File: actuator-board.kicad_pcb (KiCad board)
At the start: 4 copper layers, 22 x 40 mm, 56 parts, among them J1 SERVO DCDC 5V, J10 Servo, J2 Conn_01x06, J3 Actuator1, J4 Actuator2, J5 SWD/DEBUG, J6 BATTERY, J7 CAN, J8 CAN, J9 Servo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

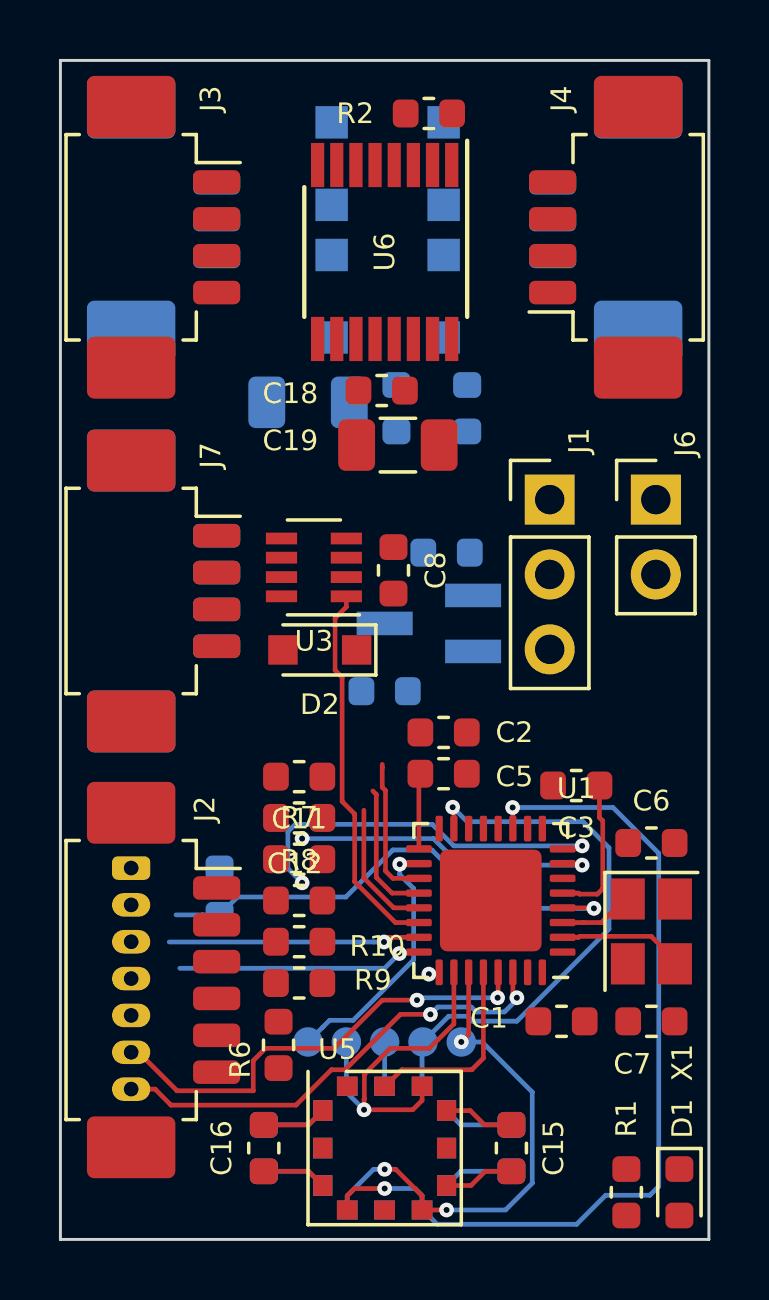
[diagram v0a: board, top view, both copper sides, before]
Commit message: layout: CAN, rearrange LED/CS1/CS2
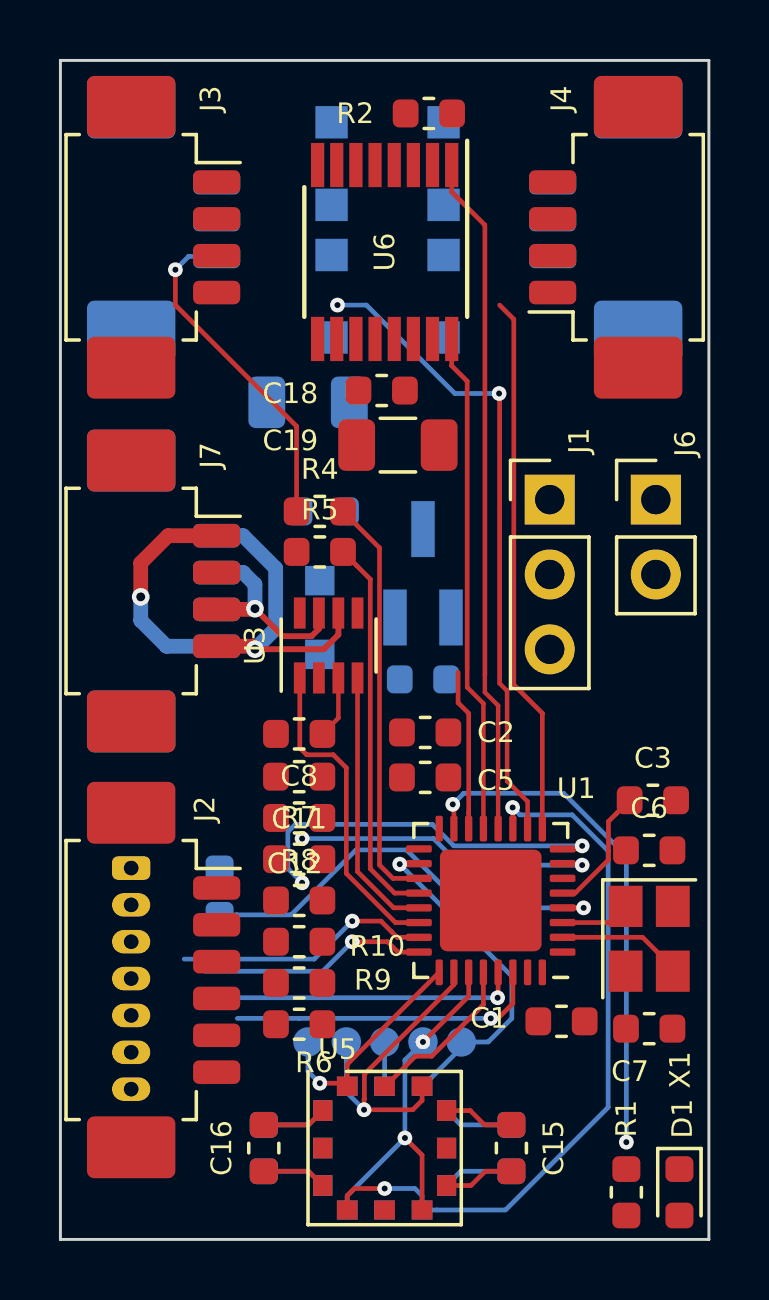
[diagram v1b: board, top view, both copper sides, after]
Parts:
- D2: moved to B.Cu
- R4, R5: moved to F.Cu
- moved R5 6.98 mm to (56.8, 76.7), turned to 0 degrees
- moved C8 6.41 mm to (56.1, 82.8), turned to 180 degrees
- moved C9 4.43 mm to (56.9, 75.3), turned to 180 degrees
- moved R4 4.36 mm to (56.8, 75.3), turned to 0 degrees
- moved U3 2.70 mm to (57.1, 79.8), turned to 90 degrees
- moved C3 2.65 mm to (68.1, 85.1), turned to 0 degrees
- moved U2 1.71 mm to (60.3, 77.4), turned to 90 degrees
- moved C10 1.36 mm to (60.3, 81.0)
- moved TP2 1.30 mm to (60.3, 93.3)
- moved TP4 1.30 mm to (61.6, 93.3)
- moved D2 1.10 mm to (56.8, 78.9), turned to 270 degrees
- moved R6 0.99 mm to (56.1, 92.7), turned to 0 degrees
- moved C5 0.64 mm to (60.4, 84.3)
- moved C2 0.62 mm to (60.4, 82.8)
- moved C6 0.26 mm to (68.0, 86.8)
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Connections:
- U1 pad 15: /SPI_CS1 -> /LED
- U1 pad 18: /SPI_CS2 -> /SPI_CS1
- U1 pad 25: /LED -> /SPI_CS2
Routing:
- net /PUMP_SOLENOID_ENABLE: track 0.00 -> 23.2 mm
- net /SOLENOID_IN2: track 0.00 -> 21.9 mm, vias 0 -> 2
- net /SOLENOID_IN1: track 0.00 -> 18.4 mm
- net /LED: track 0.38 -> 17.5 mm, vias 1 -> 2
- net /PUMP1: track 0.00 -> 17.1 mm
- net /SERVO1: track 0.00 -> 11.5 mm, vias 0 -> 1
- net Net-(J7-Pad4): track 0.00 -> 10.6 mm, vias 0 -> 1
- net Net-(R4-Pad2): track 4.90 -> 14.0 mm
- net Net-(R5-Pad2): track 4.65 -> 13.1 mm
- net +5V: track 0.00 -> 7.85 mm, vias 0 -> 1
- net /SPI_CS1: track 18.9 -> 11.7 mm
- net Net-(J7-Pad3): track 0.00 -> 6.79 mm, vias 0 -> 1
- net /PUMP2: track 0.00 -> 5.45 mm
- net /VACUUM_SENS_RESET: track 30.1 -> 24.7 mm
- net /UART1RX: track 15.9 -> 10.6 mm, vias 2 -> 1
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
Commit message: layout: power electronics, more components on F.Cu layer
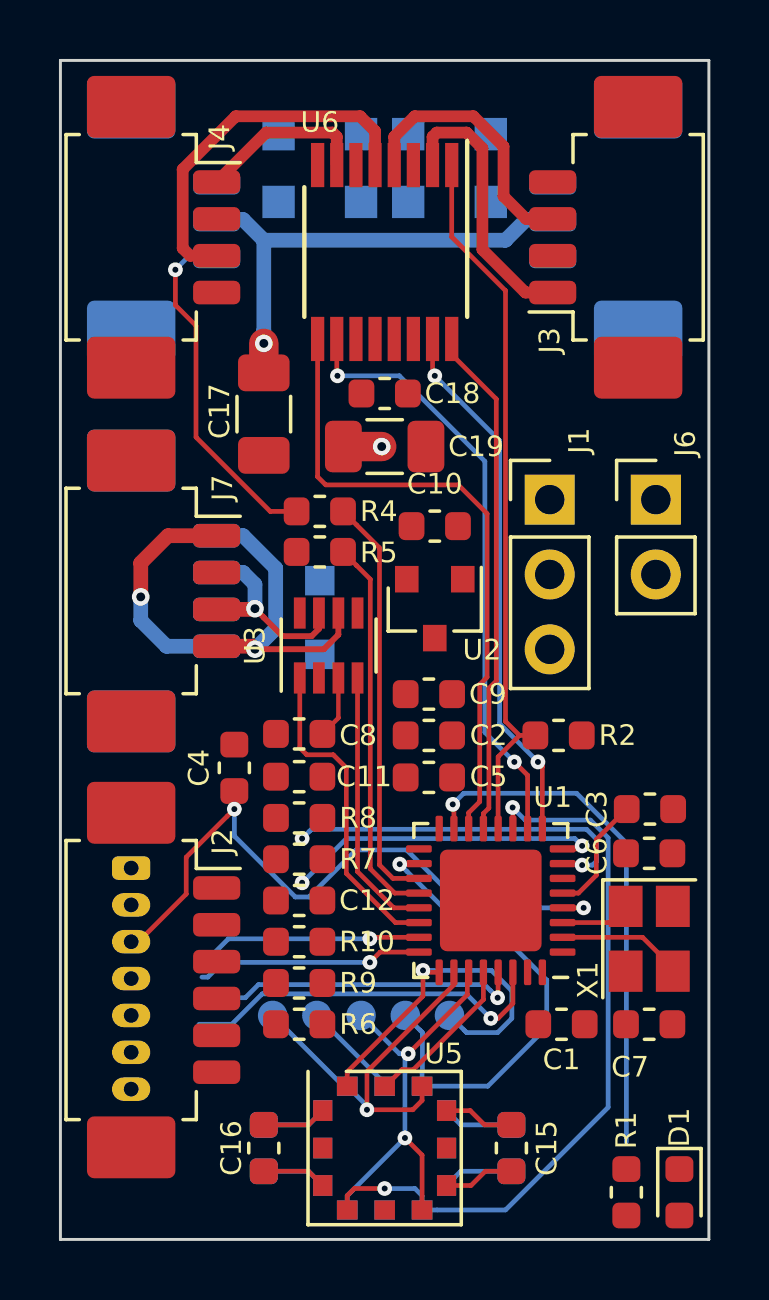
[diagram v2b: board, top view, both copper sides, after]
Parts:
- C10, C17, C4, C9: moved to F.Cu
- U2: footprint Package_TO_SOT_SMD:SOT-23_Handsoldering -> Package_TO_SOT_SMD:SOT-23; moved to F.Cu
- moved R2 21.6 mm to (64.9, 82.9), turned to 0 degrees
- moved J3 16.2 mm to (67.1, 66.0), turned to 90 degrees
- moved J4 16.2 mm to (50.9, 66.0), turned to 270 degrees
- moved C9 7.17 mm to (60.5, 81.5), turned to 0 degrees
- moved D5 6.92 mm to (56.8, 62.5), turned to 0 degrees
- moved C10 5.22 mm to (60.7, 75.8)
- moved D3 5.12 mm to (61.2, 64.8), turned to 180 degrees
- moved TP5 4.88 mm to (61.2, 92.4)
- moved D6 4.40 mm to (56.8, 64.8), turned to 0 degrees
- moved C4 4.23 mm to (53.9, 84.0)
- moved D4 4.12 mm to (61.2, 62.5), turned to 180 degrees
- moved TP3 2.66 mm to (55.2, 92.4)
- moved TP1 2.47 mm to (56.7, 92.4)
- moved TP2 2.28 mm to (58.2, 92.4)
- moved TP4 2.10 mm to (59.7, 92.4)
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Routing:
- net Net-(C17-Pad1): track 0.00 -> 34.3 mm, vias 0 -> 1
- net /PUMP2: track 5.45 -> 21.9 mm
- net Net-(D6-Pad1): track 0.00 -> 12.6 mm
- net +BATT: track 0.00 -> 11.3 mm, vias 0 -> 1
- net Net-(D3-Pad1): track 0.00 -> 9.35 mm
- net Net-(D4-Pad1): track 0.00 -> 9.05 mm
- net /RESET: track 14.8 -> 22.5 mm, vias 1 -> 2
- net Net-(D5-Pad1): track 0.00 -> 5.79 mm
- net /SPI_CS1: track 11.7 -> 16.7 mm
- net /SPI_CS2: track 7.69 -> 12.4 mm
- net /SPI_MISO: track 12.5 -> 14.6 mm
- net /ANALOG2: track 13.0 -> 10.9 mm
- net /UART1RX: track 10.6 -> 12.7 mm
- net /SPI_SCK: track 11.1 -> 13.0 mm
- net /SPI_MOSI: track 7.09 -> 8.85 mm
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
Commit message: HTSSOP motor driver, component arrangment, added MCU capacitor
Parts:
- added C20: 1uF, Capacitor_SMD:C_0603_1608Metric, F.Cu at (68.0, 84.6)
- C3: value 0.1uF -> 10nF
- D2: moved to F.Cu
- U6: footprint Package_SO:TSSOP-16_4.4x5mm_P0.65mm -> Package_SO:TSSOP-16-1EP_4.4x5mm_P0.65mm
- moved R2 11.7 mm to (63.8, 71.3)
- moved C17 11.2 mm to (66.0, 73.6), turned to 0 degrees
- moved R4 7.22 mm to (60.5, 81.5), turned to 180 degrees
- moved D2 7.18 mm to (54.8, 72.0), turned to 90 degrees
- moved C9 7.03 mm to (56.0, 76.1), turned to 270 degrees
- moved J1 6.90 mm to (64.6, 81.8), turned to 180 degrees
- moved J6 6.90 mm to (68.2, 81.8), turned to 180 degrees
- moved R5 5.04 mm to (60.5, 80.1), turned to 180 degrees
- moved U2 2.92 mm to (59.2, 76.1), turned to 180 degrees
- moved C10 1.22 mm to (61.9, 76.0), turned to 270 degrees
- moved C1 0.78 mm to (64.5, 93.3)
- moved C3 0.60 mm to (68.0, 86.0)
- moved X1 0.53 mm to (67.8, 90.3)
- moved C6 0.50 mm to (68.0, 87.4)
- moved C7 0.50 mm to (68.0, 93.2)
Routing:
- net Net-(C17-Pad1): track 34.3 -> 0.00 mm, vias 1 -> 0
- net /PUMP2: track 21.9 -> 5.04 mm
- net /SERVO1: track 12.0 -> 0.00 mm, vias 1 -> 0
- net +BATT: track 11.3 -> 0.00 mm, vias 1 -> 0
- net Net-(R4-Pad2): track 14.0 -> 7.52 mm
- net VCC: track 10.8 -> 6.72 mm
- net /RESET: track 22.5 -> 18.7 mm
- net Net-(R5-Pad2): track 13.1 -> 9.64 mm
- net /UART1RX: track 12.7 -> 15.9 mm
- net /PUMP_SOLENOID_ENABLE: track 24.3 -> 23.2 mm

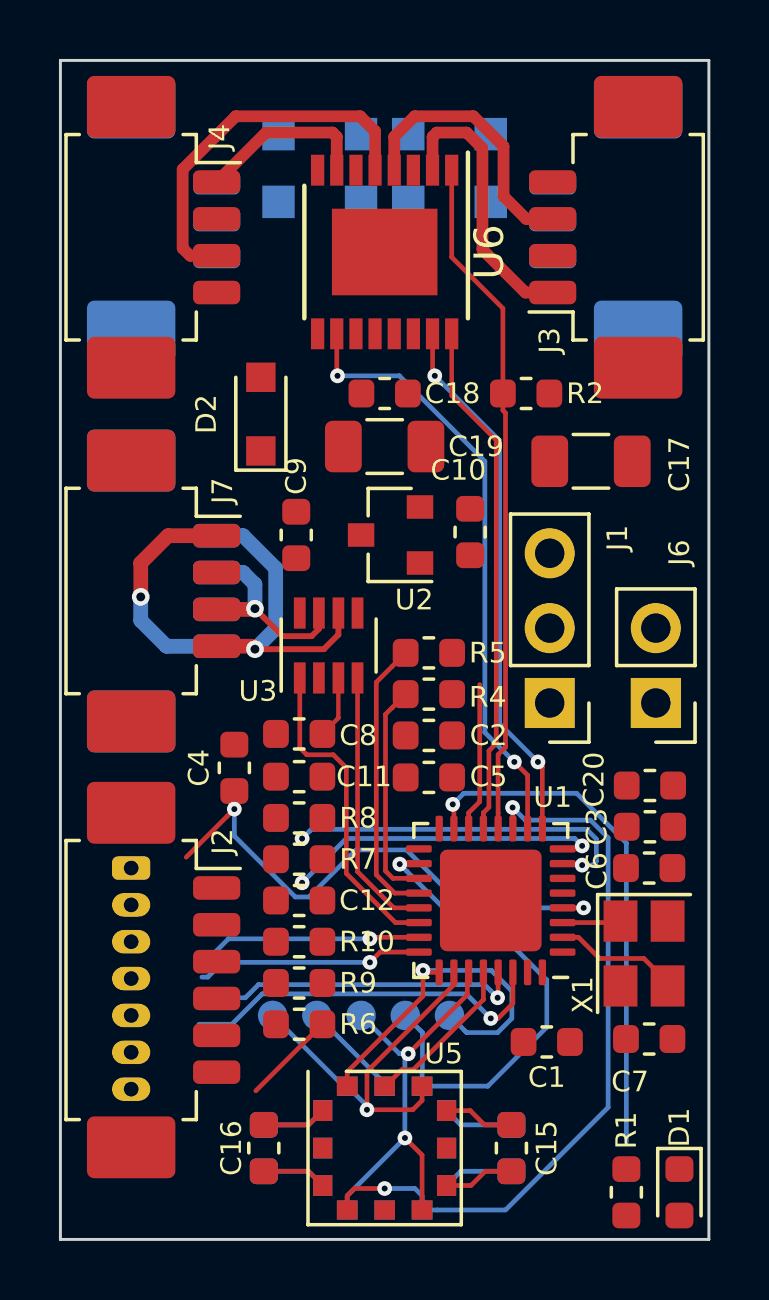
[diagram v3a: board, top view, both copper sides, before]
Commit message: Silk screen doc, ground vias, exchange servo 1 <-> 2
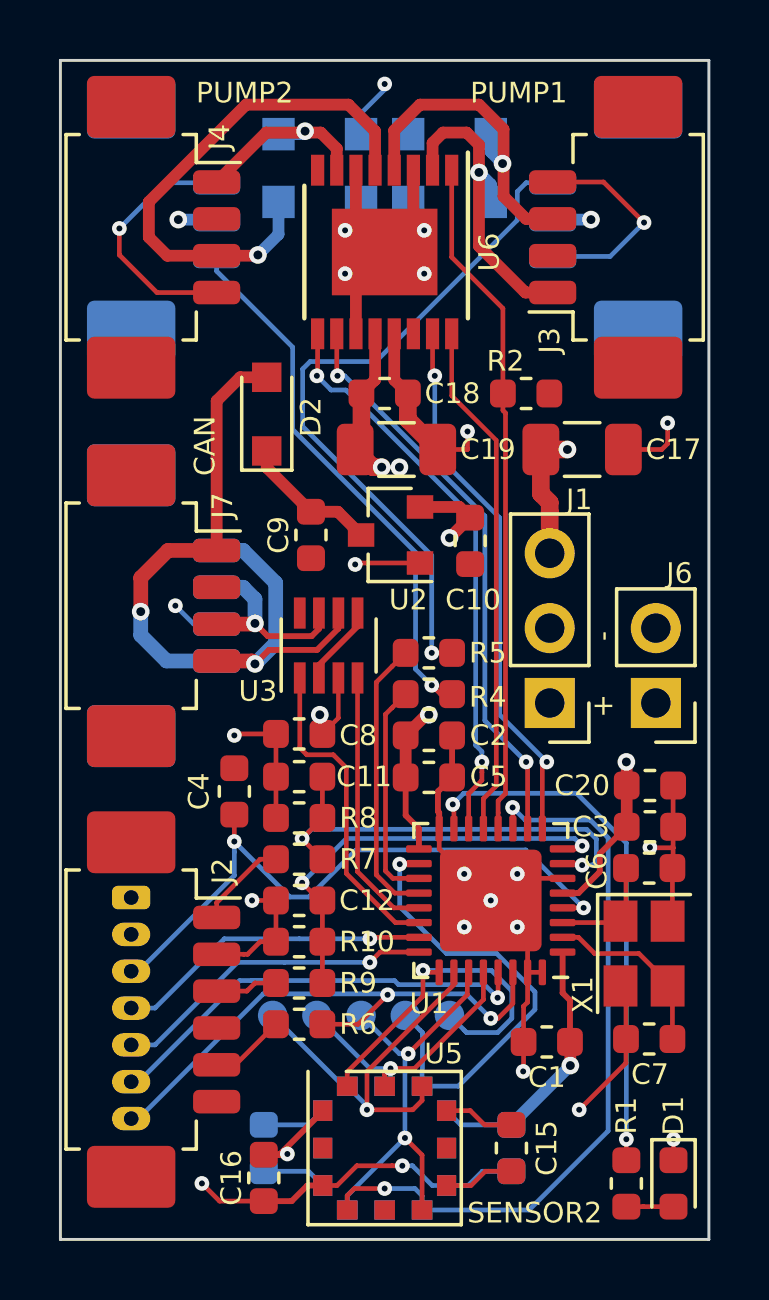
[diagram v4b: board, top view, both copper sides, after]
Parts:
- added G1: LOGO, _logo:CVRA-logo-small, B.Cu at (56.2, 69.9)
- moved C16 1.01 mm to (54.9, 97.9)
- moved J2 1.00 mm to (50.9, 92.2)
- moved J5 1.00 mm to (50.4, 88.4)
- moved C4 0.80 mm to (53.9, 84.8)
- moved C9 0.50 mm to (56.5, 76.1)
- moved J7 0.50 mm to (50.9, 78.5)
- moved J8 0.50 mm to (50.9, 78.5)
- moved C17 0.50 mm to (65.7, 73.2)
- moved C19 0.41 mm to (59.4, 73.2)
- moved D1 0.36 mm to (68.8, 98.1)
- moved R1 0.30 mm to (67.2, 98.1)
- moved C10 0.30 mm to (61.9, 76.3)
- moved D2 0.20 mm to (55.0, 72.0)
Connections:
- J10 pad 1: /SERVO2 -> /SERVO1
- J9 pad 1: /SERVO1 -> /SERVO2
- R4 pad 1: /SERVO1 -> /SERVO2
- R5 pad 1: /SERVO2 -> /SERVO1
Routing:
- net GND: track 4.60 -> 92.4 mm, vias 0 -> 24
- net VCC: track 6.72 -> 85.4 mm, vias 0 -> 6
- net Net-(C17-Pad1): track 0.00 -> 29.8 mm, vias 0 -> 3
- net /SERVO1: track 0.00 -> 23.8 mm, vias 0 -> 1
- net +BATT: track 0.00 -> 20.8 mm, vias 0 -> 2
- net /SERVO2: track 0.00 -> 18.4 mm, vias 0 -> 1
- net /PUMP2: track 5.04 -> 19.6 mm, vias 0 -> 2
- net +5V: track 7.85 -> 15.0 mm
- net Net-(D6-Pad1): track 12.6 -> 18.0 mm, vias 0 -> 1
- net Net-(C9-Pad1): track 0.00 -> 4.71 mm
- net /UART1TX: track 11.5 -> 15.7 mm
- net /ANALOG2: track 10.9 -> 14.7 mm
- net /ANALOG1: track 12.3 -> 15.7 mm
- net /SWCK: track 7.71 -> 11.1 mm
- net /UART1RX: track 15.9 -> 19.2 mm, vias 1 -> 2
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- added copper zone on B.Cu, net GND
- added copper zone on F.Cu, net GND
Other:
- board text added: "+"
- board text added: "-"
- board text added: "5V Servo"
- board text added: "Actuator board RevA"
- board text added: "Authors: M. Spieler S. Missri A. Albertelli"
- board text added: "CAN"
- board text added: "CS1"
- board text added: "CS2"
- board text added: "CVRA"
- board text added: "GND"
- board text added: "MISO"
- board text added: "MOSI"
- board text added: "PUMP1"
- board text added: "PUMP2"
- board text added: "RST"
- board text added: "RX"
- board text added: "SCK"
- board text added: "SENSOR1"
- board text added: "SENSOR2"
- board text added: "SERVO1"
- board text added: "SERVO2"
- board text added: "SWCK"
- board text added: "SWIO"
- board text added: "TX"
- board text added: "VBAT"
- board text added: "VCC"

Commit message: Changes from review: move C2, move VCC via, add fiducials, component placement
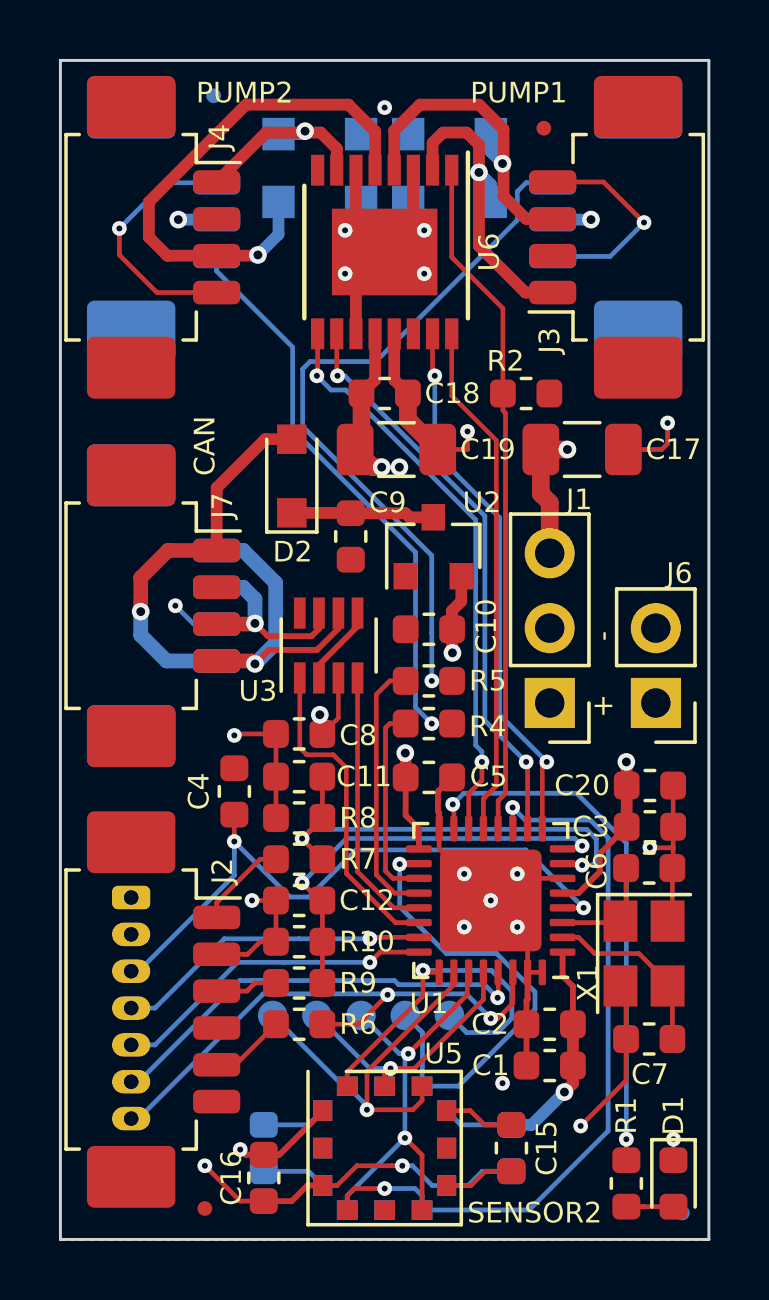
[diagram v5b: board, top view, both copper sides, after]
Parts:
- added FID1: Fiducial, Fiducial:Fiducial_0.5mm_Mask1mm, F.Cu at (52.9, 99.0)
- added FID2: Fiducial, Fiducial:Fiducial_0.5mm_Mask1mm, F.Cu at (64.4, 62.3)
- added FID3: Fiducial, Fiducial:Fiducial_0.5mm_Mask1mm, B.Cu at (69.1, 99.1)
- added FID4: Fiducial, Fiducial:Fiducial_0.5mm_Mask1mm, B.Cu at (53.2, 61.2)
- moved C2 10.6 mm to (64.6, 92.7), turned to 180 degrees
- moved C10 3.31 mm to (60.5, 79.3), turned to 180 degrees
- moved D2 2.27 mm to (55.9, 74.1)
- moved U2 1.50 mm to (60.6, 76.5), turned to 90 degrees
- moved C9 1.35 mm to (57.9, 76.2)
- moved R4 1.00 mm to (60.5, 82.5)
- moved R5 0.95 mm to (60.5, 81.0)
- moved C1 0.81 mm to (64.6, 94.1)
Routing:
- net VCC: track 85.4 -> 27.9 mm
- net GND: track 92.4 -> 87.1 mm, vias 24 -> 23
- net +5V: track 15.0 -> 13.2 mm
- net /SERVO2: track 18.4 -> 19.6 mm
- net /SERVO1: track 23.8 -> 24.9 mm
- net Net-(R4-Pad2): track 7.52 -> 6.83 mm
- net Net-(R5-Pad2): track 9.64 -> 9.01 mm
